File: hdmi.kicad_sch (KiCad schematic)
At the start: 58 parts, among them J13 WE_685119136923_alt_sym, Q1 PJE138K, Q12 PJE138K, Q2 PJE138K, Q3 PJE138K, U36 TS3DV642RUARQ1, U43 NTS0102GT, U44 TPD4E05U06QDQARQ1, U45 TPD4E05U06QDQARQ1, U46 TPD4E05U06QDQARQ1

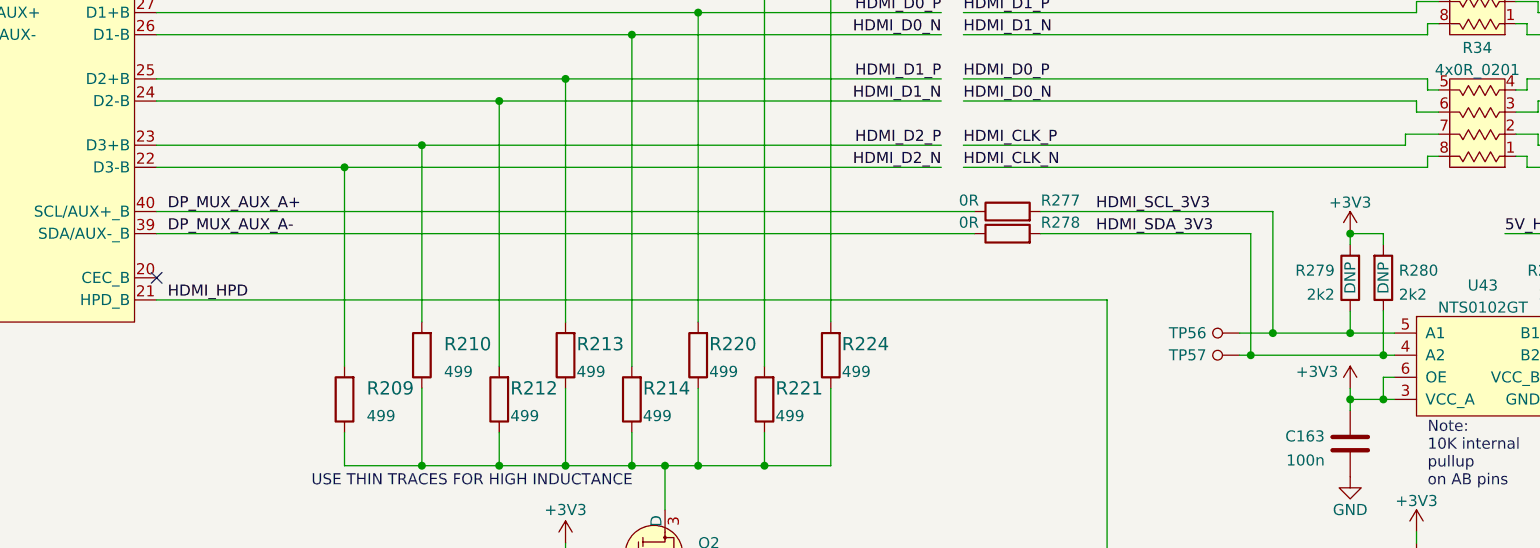
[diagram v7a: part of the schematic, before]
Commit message: Fix SDA/SCL cross
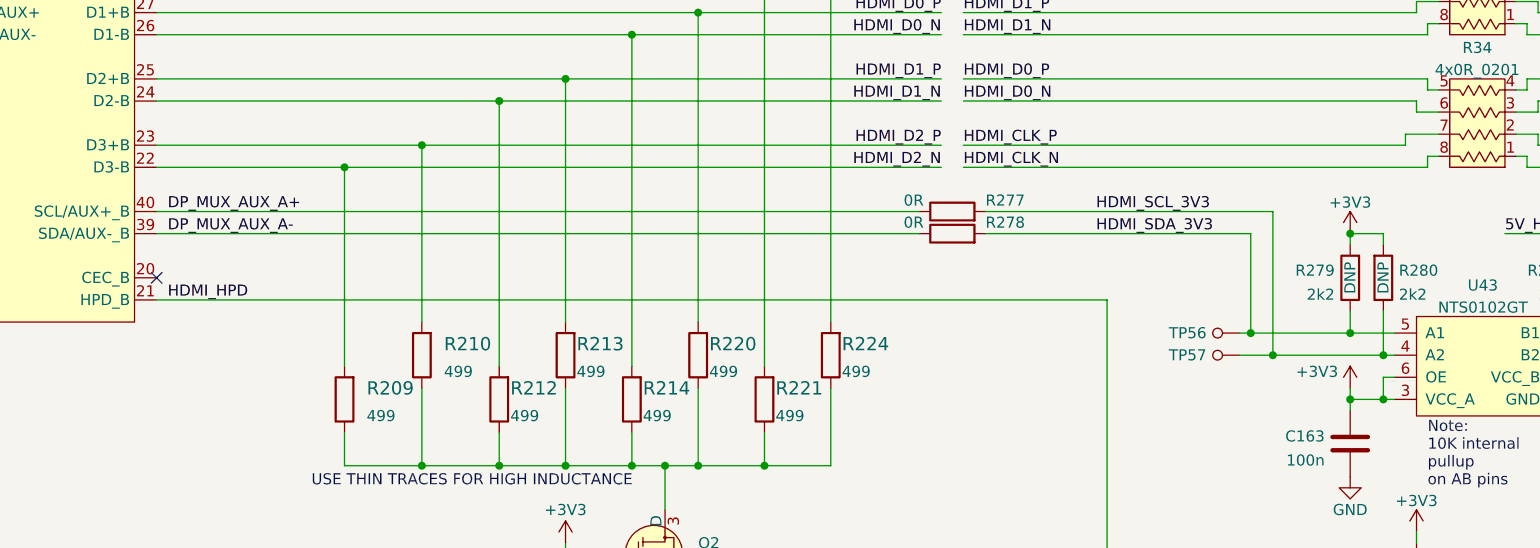
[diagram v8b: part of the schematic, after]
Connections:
- net HDMI_SCL_3V3: now also R280.1, TP57.1, U43.4 (A2); no longer R279.1, TP56.1, U43.5 (A1)
- net HDMI_SDA_3V3: now also R279.1, TP56.1, U43.5 (A1); no longer R280.1, TP57.1, U43.4 (A2)
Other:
- moved on the sheet: R277, R278
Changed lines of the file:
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@@
   (junction (at 186.69 196.85) (diameter 0) (color 0 0 0 0)
   )
-  (junction (at 250.19 184.15) (diameter 0) (color 0 0 0 0)
-  )
   (junction (at 269.24 215.9) (diameter 0) (color 0 0 0 0)
   )
@@
   (junction (at 171.45 196.85) (diameter 0) (color 0 0 0 0)
   )
-  (junction (at 252.73 181.61) (diameter 0) (color 0 0 0 0)
-  )
   (junction (at 163.83 196.85) (diameter 0) (color 0 0 0 0)
   )
@@
   (junction (at 265.43 184.15) (diameter 0) (color 0 0 0 0)
   )
+  (junction (at 250.19 181.61) (diameter 0) (color 0 0 0 0)
+  )
   (junction (at 194.31 196.85) (diameter 0) (color 0 0 0 0)
   )
@@
   (junction (at 186.69 144.78) (diameter 0) (color 0 0 0 0)
   )
+  (junction (at 252.73 184.15) (diameter 0) (color 0 0 0 0)
+  )
   (junction (at 93.98 170.18) (diameter 0) (color 0 0 0 0)
   )
@@
     (stroke (width 0) (type default) (color 0 0 0 0))
   )
-  (wire (pts (xy 248.92 184.15) (xy 250.19 184.15))
+  (wire (pts (xy 248.92 184.15) (xy 252.73 184.15))
     (stroke (width 0) (type default) (color 0 0 0 0))
   )
@@
     (stroke (width 0) (type default) (color 0 0 0 0))
   )
+  (wire (pts (xy 250.19 181.61) (xy 261.62 181.61))
+    (stroke (width 0) (type default) (color 0 0 0 0))
+  )
   (wire (pts (xy 74.93 124.46) (xy 99.06 124.46))
     (stroke (width 0) (type default) (color 0 0 0 0))
@@
     (stroke (width 0) (type default) (color 0 0 0 0))
   )
-  (wire (pts (xy 248.92 181.61) (xy 252.73 181.61))
+  (wire (pts (xy 248.92 181.61) (xy 250.19 181.61))
     (stroke (width 0) (type default) (color 0 0 0 0))
   )
@@
     (stroke (width 0) (type default) (color 0 0 0 0))
   )
-  (wire (pts (xy 271.78 158.75) (xy 267.97 158.75))
+  (wire (pts (xy 252.73 184.15) (xy 265.43 184.15))
     (stroke (width 0) (type default) (color 0 0 0 0))
   )
-  (wire (pts (xy 163.83 193.04) (xy 163.83 196.85))
+  (wire (pts (xy 271.78 158.75) (xy 267.97 158.75))
     (stroke (width 0) (type default) (color 0 0 0 0))
   )
-  (wire (pts (xy 252.73 167.64) (xy 252.73 181.61))
+  (wire (pts (xy 163.83 193.04) (xy 163.83 196.85))
     (stroke (width 0) (type default) (color 0 0 0 0))
   )
@@
     (stroke (width 0) (type default) (color 0 0 0 0))
   )
-  (wire (pts (xy 250.19 170.18) (xy 250.19 184.15))
-    (stroke (width 0) (type default) (color 0 0 0 0))
-  )
   (wire (pts (xy 124.46 139.7) (xy 194.31 139.7))
     (stroke (width 0) (type default) (color 0 0 0 0))
@@
     (stroke (width 0) (type default) (color 0 0 0 0))
   )
-  (wire (pts (xy 226.06 167.64) (xy 252.73 167.64))
+  (wire (pts (xy 219.71 167.64) (xy 252.73 167.64))
     (stroke (width 0) (type default) (color 0 0 0 0))
   )
@@
     (stroke (width 0) (type default) (color 0 0 0 0))
   )
-  (wire (pts (xy 124.46 167.64) (xy 218.44 167.64))
+  (wire (pts (xy 124.46 167.64) (xy 212.09 167.64))
     (stroke (width 0) (type default) (color 0 0 0 0))
   )
@@
     (stroke (width 0) (type default) (color 0 0 0 0))
   )
-  (wire (pts (xy 250.19 184.15) (xy 265.43 184.15))
-    (stroke (width 0) (type default) (color 0 0 0 0))
-  )
   (wire (pts (xy 283.21 156.21) (xy 283.21 154.94))
     (stroke (width 0) (type default) (color 0 0 0 0))
@@
     (stroke (width 0) (type default) (color 0 0 0 0))
   )
-  (wire (pts (xy 226.06 170.18) (xy 250.19 170.18))
+  (wire (pts (xy 219.71 170.18) (xy 250.19 170.18))
     (stroke (width 0) (type default) (color 0 0 0 0))
   )
@@
     (stroke (width 0) (type default) (color 0 0 0 0))
   )
+  (wire (pts (xy 252.73 167.64) (xy 252.73 184.15))
+    (stroke (width 0) (type default) (color 0 0 0 0))
+  )
   (wire (pts (xy 171.45 196.85) (xy 179.07 196.85))
     (stroke (width 0) (type default) (color 0 0 0 0))
@@
     (stroke (width 0) (type default) (color 0 0 0 0))
   )
-  (wire (pts (xy 124.46 170.18) (xy 218.44 170.18))
+  (wire (pts (xy 124.46 170.18) (xy 212.09 170.18))
     (stroke (width 0) (type default) (color 0 0 0 0))
   )
@@
     (stroke (width 0) (type default) (color 0 0 0 0))
   )
-  (wire (pts (xy 252.73 181.61) (xy 261.62 181.61))
-    (stroke (width 0) (type default) (color 0 0 0 0))
-  )
   (wire (pts (xy 283.21 139.7) (xy 353.06 139.7))
     (stroke (width 0) (type default) (color 0 0 0 0))
@@
     (stroke (width 0) (type default) (color 0 0 0 0))
   )
+  (wire (pts (xy 250.19 170.18) (xy 250.19 181.61))
+    (stroke (width 0) (type default) (color 0 0 0 0))
+  )
   (wire (pts (xy 314.96 53.34) (xy 313.69 53.34))
     (stroke (width 0) (type default) (color 0 0 0 0))
@@
     (pin "2")
   )
-  (symbol (lib_id "jetson-orin-baseboard:R_0R_0402") (at 222.25 167.64 0) (unit 1)
+  (symbol (lib_id "jetson-orin-baseboard:R_0R_0402") (at 215.9 167.64 0) (unit 1)
     (in_bom yes) (on_board yes)
-    (property "Reference" "R277" (id 0) (at 226.06 166.37 0)
+    (property "Reference" "R277" (id 0) (at 219.71 166.37 0)
       (effects (font (size 1.27 1.27)) (justify left))
     )
-    (property "Value" "R_0R_0402" (id 1) (at 222.25 171.45 0)
+    (property "Value" "R_0R_0402" (id 1) (at 215.9 171.45 0)
       (effects (font (size 1.27 1.27)) hide)
     )
-    (property "Footprint" "jetson-orin-baseboard-footprints:0402-res" (id 2) (at 227.33 162.56 0)
+    (property "Footprint" "jetson-orin-baseboard-footprints:0402-res" (id 2) (at 220.98 162.56 0)
       (effects (font (size 1.524 1.524)) (justify left) hide)
     )
-    (property "Datasheet" "" (id 3) (at 222.25 167.64 0)
+    (property "Datasheet" "" (id 3) (at 215.9 167.64 0)
       (effects (font (size 1.27 1.27)) hide)
     )
-    (property "Manufacturer" "PANASONIC" (id 4) (at 227.33 157.48 0)
+    (property "Manufacturer" "PANASONIC" (id 4) (at 220.98 157.48 0)
       (effects (font (size 1.524 1.524)) (justify left) hide)
     )
-    (property "MPN" "ERJ2GE0R00X" (id 5) (at 227.33 160.02 0)
+    (property "MPN" "ERJ2GE0R00X" (id 5) (at 220.98 160.02 0)
       (effects (font (size 1.524 1.524)) (justify left) hide)
     )
-    (property "Val" "0R" (id 6) (at 217.805 166.37 0))
+    (property "Val" "0R" (id 6) (at 211.455 166.37 0))
     (pin "1")
     (pin "2")
@@
     (pin "2")
   )
-  (symbol (lib_id "jetson-orin-baseboard:R_0R_0402") (at 222.25 170.18 0) (unit 1)
+  (symbol (lib_id "jetson-orin-baseboard:R_0R_0402") (at 215.9 170.18 0) (unit 1)
     (in_bom yes) (on_board yes)
-    (property "Reference" "R278" (id 0) (at 226.06 168.91 0)
+    (property "Reference" "R278" (id 0) (at 219.71 168.91 0)
       (effects (font (size 1.27 1.27)) (justify left))
     )
-    (property "Value" "R_0R_0402" (id 1) (at 222.25 173.99 0)
+    (property "Value" "R_0R_0402" (id 1) (at 215.9 173.99 0)
       (effects (font (size 1.27 1.27)) hide)
     )
-    (property "Footprint" "jetson-orin-baseboard-footprints:0402-res" (id 2) (at 227.33 165.1 0)
+    (property "Footprint" "jetson-orin-baseboard-footprints:0402-res" (id 2) (at 220.98 165.1 0)
       (effects (font (size 1.524 1.524)) (justify left) hide)
     )
-    (property "Datasheet" "" (id 3) (at 222.25 170.18 0)
+    (property "Datasheet" "" (id 3) (at 215.9 170.18 0)
       (effects (font (size 1.27 1.27)) hide)
     )
-    (property "Manufacturer" "PANASONIC" (id 4) (at 227.33 160.02 0)
+    (property "Manufacturer" "PANASONIC" (id 4) (at 220.98 160.02 0)
       (effects (font (size 1.524 1.524)) (justify left) hide)
     )
-    (property "MPN" "ERJ2GE0R00X" (id 5) (at 227.33 162.56 0)
+    (property "MPN" "ERJ2GE0R00X" (id 5) (at 220.98 162.56 0)
       (effects (font (size 1.524 1.524)) (justify left) hide)
     )
-    (property "Val" "0R" (id 6) (at 217.805 168.91 0))
+    (property "Val" "0R" (id 6) (at 211.455 168.91 0))
     (pin "1")
     (pin "2")
